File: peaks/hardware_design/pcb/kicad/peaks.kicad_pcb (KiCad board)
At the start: 2 copper layers, 38.7 x 106.7 mm, 91 parts, among them IC1 REG1117, IC2 LM4041DBZ, IC3 DAC8552, IC4 TL072D, IC5 TL072D, IC6 LM4041DBZ, J1 PJ301_THONKICONN6, J2 PJ301_THONKICONN6, J3 PJ301_THONKICONN6, J4 PJ301_THONKICONN6, Q1 8MHz, Q2 MMBT3904, Q3 MMBT3904, SW1 TAC_SWITCHPTH, SW2 TAC_SWITCHPTH, SW3 EVQQ2, SW4 LP4OA1PBCT, SW5 EVQQ2, SW6 LP4OA1PBCT

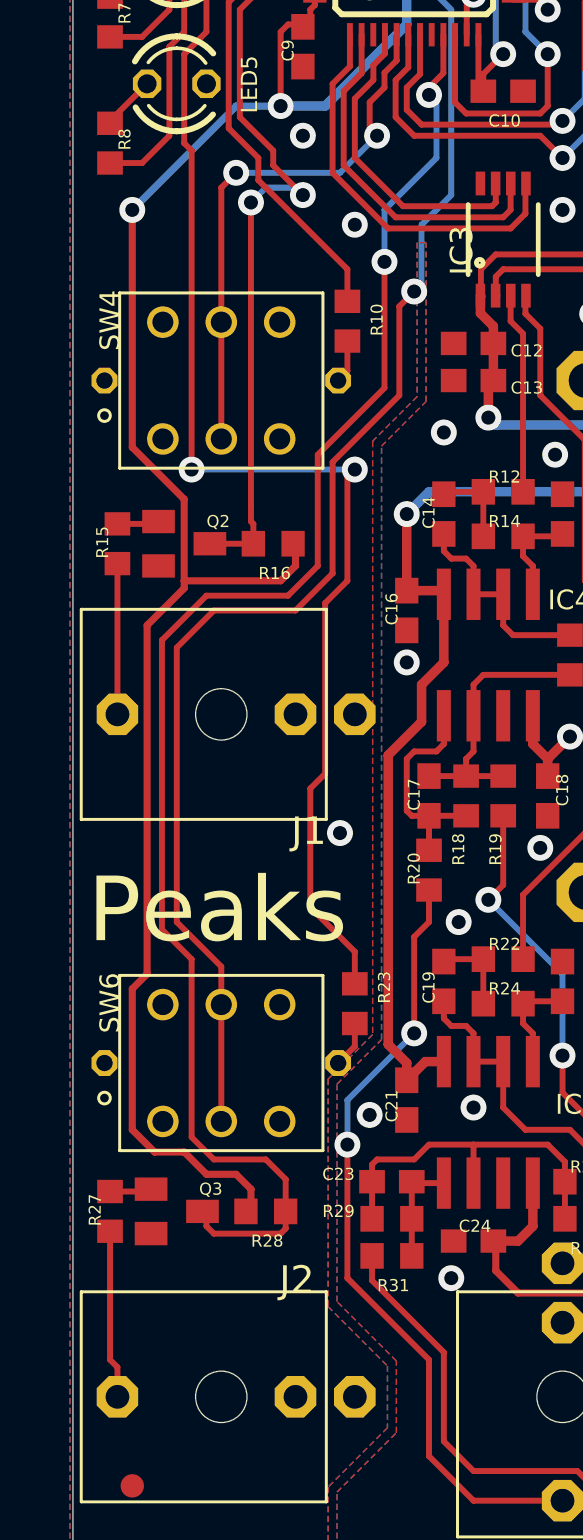
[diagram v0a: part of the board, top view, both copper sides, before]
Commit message: peaks: led/button footprint change
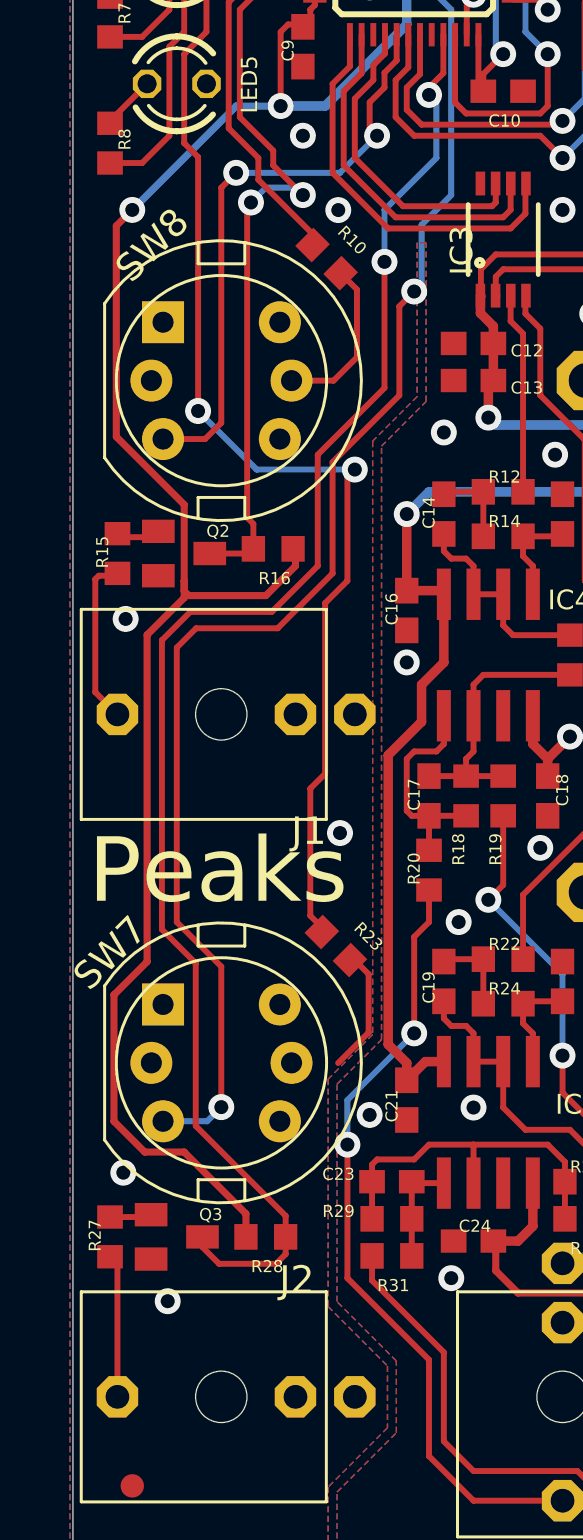
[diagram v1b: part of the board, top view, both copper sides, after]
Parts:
- removed SW4, SW6: LP4OA1PBCT, peaks:LP4OA1PBCT
- added SW7: SW_Push_LED, Library:C&K_D6R, F.Cu at (135.5, 137.7)
- added SW8: SW_Push_LED, Library:C&K_D6R, F.Cu at (135.5, 108.5)
- moved R10 2.80 mm to (140.0, 103.3), turned to 135 degrees
- moved R23 2.60 mm to (140.4, 132.7), turned to 135 degrees
- moved Q3 1.09 mm to (133.6, 145.1)
- moved R27 1.09 mm to (130.7, 145.1)
- moved R28 1.09 mm to (137.4, 145.1)
- moved Q2 0.42 mm to (133.9, 115.9)
- moved R15 0.42 mm to (131.0, 115.9)
- moved R16 0.22 mm to (137.7, 115.7)
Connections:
- R10 pad 1: Net-(R10-Pad1) -> /peaks_1/LED_TRIG_2
- R23 pad 1: Net-(R23-Pad1) -> /peaks_1/LED_TRIG_1
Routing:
- net /peaks_1/LED_TRIG_2: track 0.00 -> 7.10 mm
- net /peaks_1/LED_TRIG_1: track 0.00 -> 5.19 mm
- net Net-(UC1-PB0/ADC12_IN8/TIM3_CH3): track 58.0 -> 53.6 mm
- net Net-(UC1-PB1/ADC12_IN9/TIM3_CH4): track 20.4 -> 17.4 mm
- net +3V3: track 164.1 -> 166.5 mm
- net /peaks_1/SW_TRIG_1: track 60.4 -> 62.5 mm, vias 2 -> 3
- net /peaks_1/SW_TRIG_2: track 23.3 -> 25.4 mm
- net Net-(R23-Pad1): track 1.99 -> 0.00 mm
- net Net-(R10-Pad1): track 1.85 -> 0.00 mm
- net Net-(J2-3): track 7.22 -> 6.13 mm
- net Net-(J1-3): track 6.45 -> 7.19 mm
- net GND: vias 48 -> 51

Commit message: peaks: change led resistor from 33 to 680 ohms
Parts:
- R10, R23: value 33 -> 680
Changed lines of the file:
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@@
         (effects (font (size 0.516128 0.516128) (thickness 0.093472)) (justify left))
     )
-    (fp_text value "33" (at 0.353553 2.05061 135) (layer "F.Fab")
+    (fp_text value "680" (at 0.353553 2.05061 135) (layer "F.Fab")
         (effects (font (size 0.516128 0.516128) (thickness 0.093472)) (justify left))
     )
@@
         (effects (font (size 0.516128 0.516128) (thickness 0.093472)) (justify left))
     )
-    (fp_text value "33" (at 0 1.905 135) (layer "F.Fab")
-        (effects (font (size 0.516128 0.516128) (thickness 0.093472)) (justify left))
-    )
+    (fp_text value "680" (at 0 1.905 135) (layer "F.Fab")
+        (effects (font (size 0.516128 0.516128) (thickness 0.093472)) (justify left))
+    )

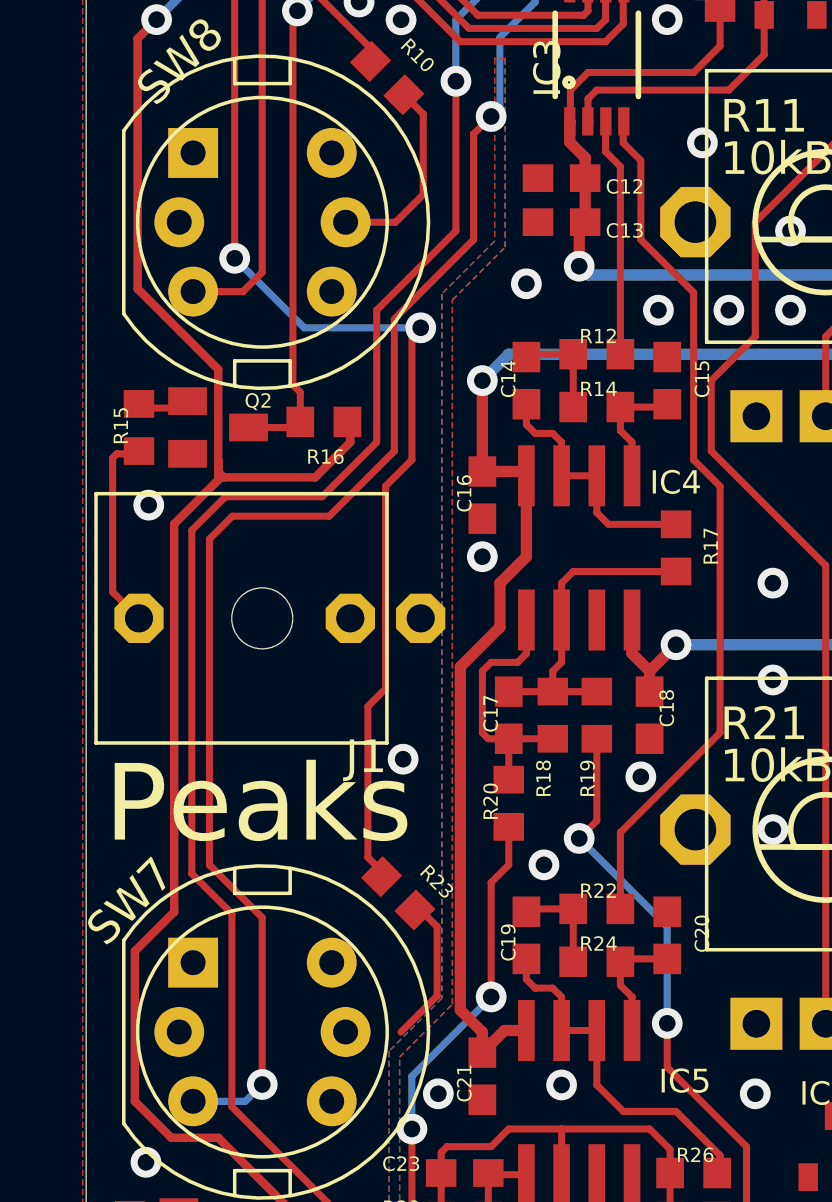
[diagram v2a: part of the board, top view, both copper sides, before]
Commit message: peaks: led button silkscren polarity
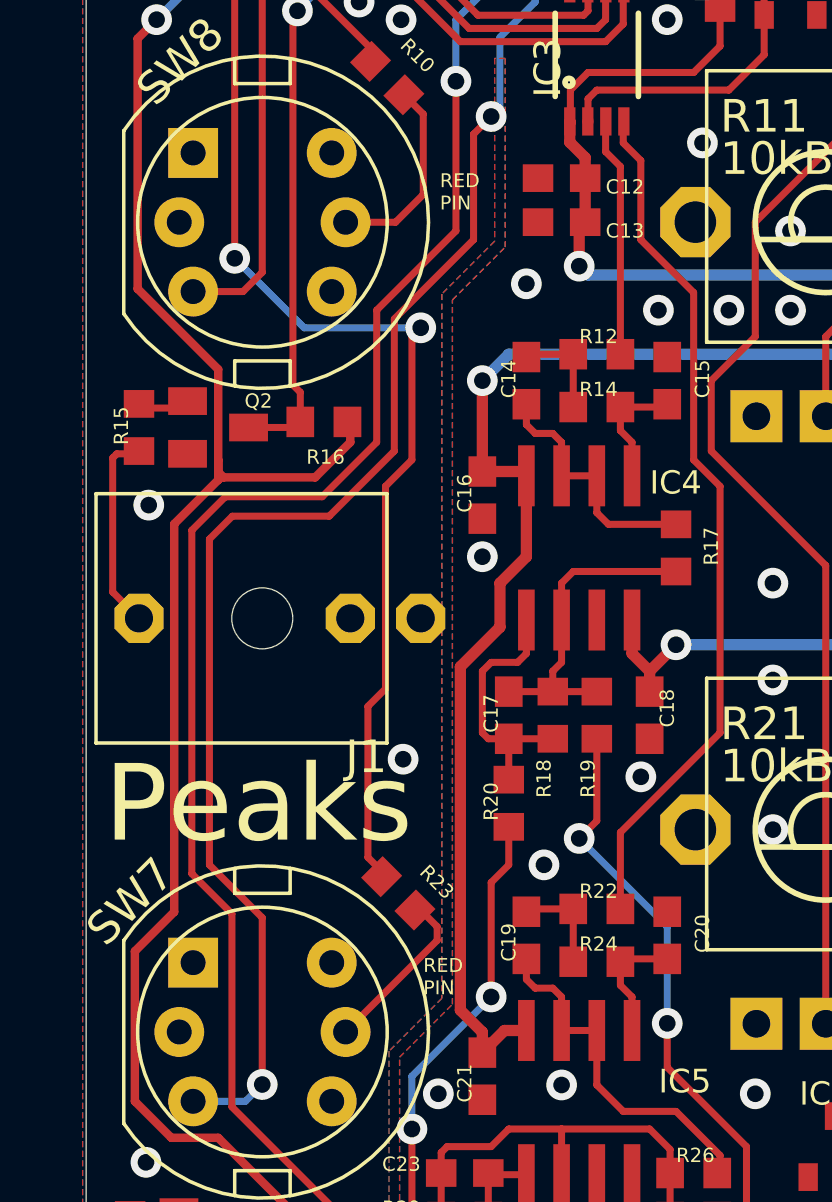
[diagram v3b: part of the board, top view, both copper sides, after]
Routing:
- net /peaks_1/LED_TRIG_1: track 5.19 -> 6.01 mm
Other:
- board text added: "RED PIN"
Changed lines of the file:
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@@
     (effects (font (size 2.76352 2.76352) (thickness 0.48768)) (justify left bottom))
+  )
+  (gr_text "RED\nPIN" (at 141.9 108.1) (layer "F.SilkS")
+    (effects (font (size 0.5 0.5) (thickness 0.1)) (justify left bottom))
   )
   (gr_text "2015. v3" (at 165.9736 112.6236 90) (layer "F.SilkS")
@@
   (gr_text "SYSBOOT" (at 167.4 131.1 90) (layer "F.SilkS")
     (effects (font (size 0.8636 0.8636) (thickness 0.1524)) (justify left bottom))
+  )
+  (gr_text "RED\nPIN" (at 141.3 136.4) (layer "F.SilkS")
+    (effects (font (size 0.5 0.5) (thickness 0.1)) (justify left bottom))
   )
   (segment (start 140.8911 91.6686) (end 140.8636 91.6961) (width 0.254) (layer "F.Cu") (net 1))
@@
   (segment (start 138.5 108.5) (end 140.3 108.5) (width 0.254) (layer "F.Cu") (net 76))
   (segment (start 141.3 104.6) (end 140.601041 103.901041) (width 0.254) (layer "F.Cu") (net 76))
-  (segment (start 141.8 136.3997) (end 141.8 133.9) (width 0.254) (layer "F.Cu") (net 77))
-  (segment (start 140.4936 137.7061) (end 141.8 136.3997) (width 0.254) (layer "F.Cu") (net 77))
   (segment (start 141.8 133.9) (end 141.202082 133.302082) (width 0.254) (layer "F.Cu") (net 77))
+  (segment (start 138.5 137.7) (end 141.8 134.4) (width 0.254) (layer "F.Cu") (net 77))
+  (segment (start 141.8 134.4) (end 141.8 133.9) (width 0.254) (layer "F.Cu") (net 77))
   (zone (net 1) (net_name "GND") (layer "F.Cu") (hatch edge 0.5)
     (priority 6)
